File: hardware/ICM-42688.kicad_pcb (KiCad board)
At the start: 2 copper layers, 35 x 25 mm, 34 parts, among them J1 Conn_01x09, Q1 BSS138, Q2 BSS138, Q3 BSS138, Q4 BSS138, U1 AMS1117-3.3, U2 ICM-42688-P

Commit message: feat: Add panelized PCB files
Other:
- board text added: "Accelerometer & Gyroscope ICM-42688 SPI/I2C Breakout Board"
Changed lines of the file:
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@@
 		(tags "capacitor tantalum")
 		(property "Reference" "C3"
-			(at 0 2.015 360)
+			(at 0 2.015 0)
 			(layer "F.SilkS")
 			(effects
@@
 		)
 		(property "Value" "2.2uF"
-			(at 0 2.35 360)
+			(at 0 2.35 0)
 			(layer "F.Fab")
 			(effects
@@
 		)
 		(fp_text user "${REFERENCE}"
-			(at 0 0 360)
+			(at 0 0 0)
 			(layer "F.Fab")
 			(effects
@@
 		(layer "Edge.Cuts")
 	)
+	(gr_text "Accelerometer & Gyroscope\nICM-42688 SPI/I2C Breakout Board"
+		(at 137.5 83.968972 0)
+		(layer "B.SilkS")
+		(effects
+			(font
+				(size 1 1)
+				(thickness 0.2)
+				(bold yes)
+			)
+			(justify bottom mirror)
+		)
+	)
 	(gr_text "SPI: V+ 3V3 DOUT DIN SCLK CS INT1 INT2 GND\nI2C: V+ 3V3 ADDR SDA SCL  NC INT1 INT2 GND"

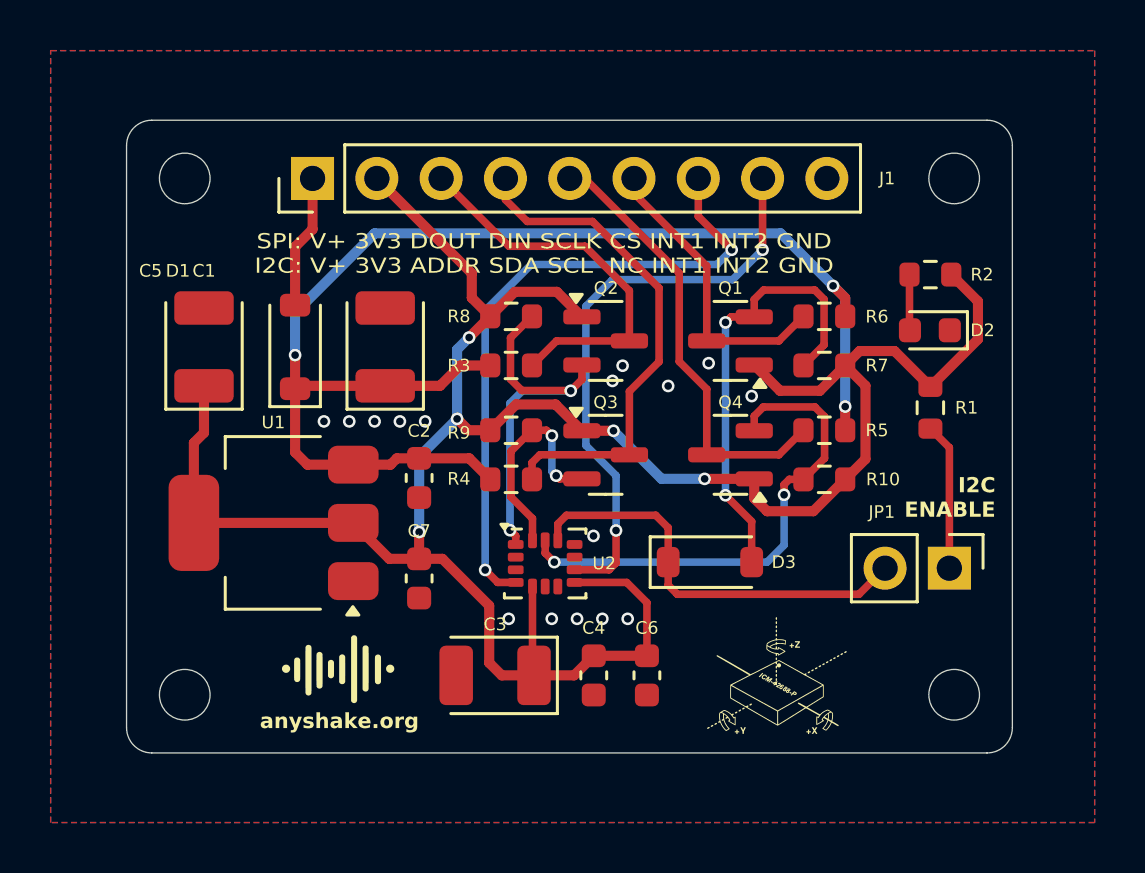
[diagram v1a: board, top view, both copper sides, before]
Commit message: fix: Fix SPI communication failure
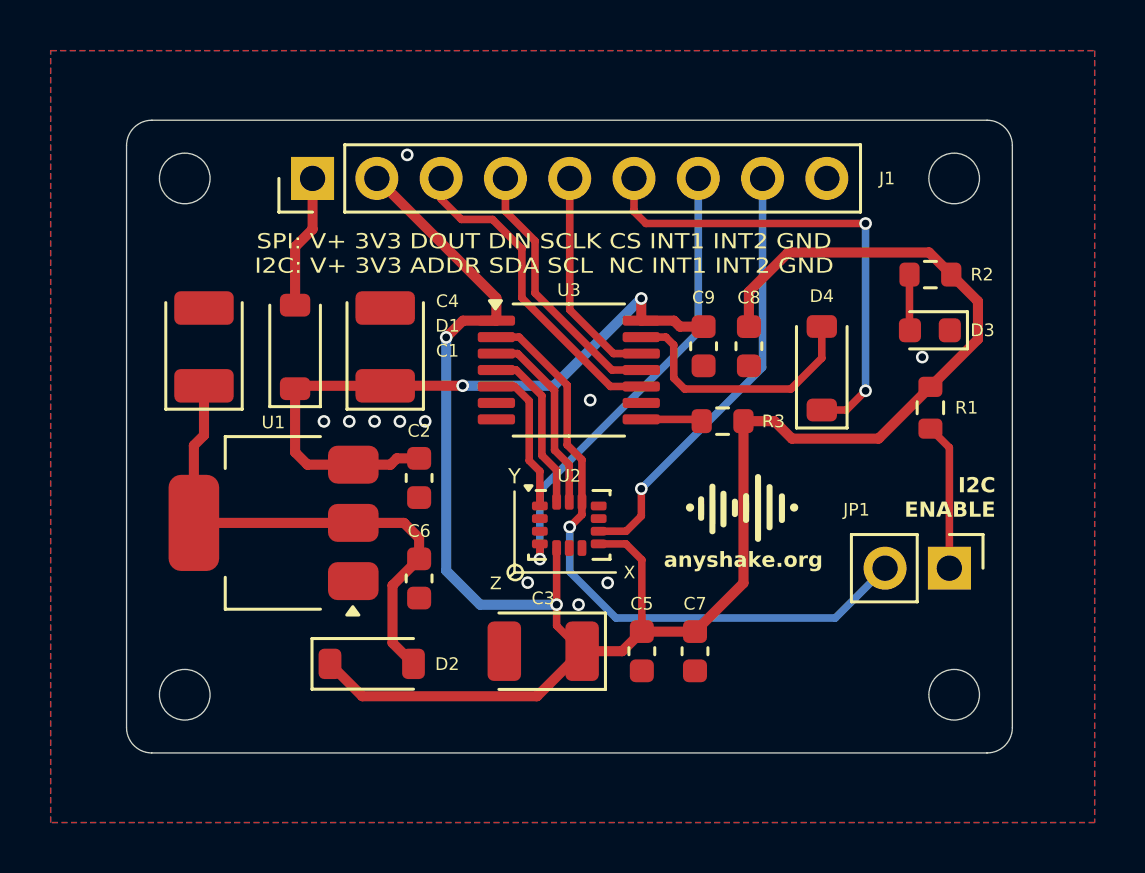
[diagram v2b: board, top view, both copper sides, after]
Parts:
- removed the D3 at (143.1, 87.5)
- removed the G*** at (145.8, 92.0)
- removed Q1, Q2, Q3, Q4: BSS138, Package_TO_SOT_SMD:SOT-23
- removed R10, R4, R5, R6, R7, R8, R9: 10k, Resistor_SMD:R_0603_1608Metric
- added C8: 0.1uF, Capacitor_SMD:C_0603_1608Metric, F.Cu at (144.6, 78.9)
- added C9: 0.1uF, Capacitor_SMD:C_0603_1608Metric, F.Cu at (142.8, 78.9)
- added D2: 1N4148, Diode_SMD:D_SOD-123, F.Cu at (129.7, 91.5)
- added D4: 1N4148, Diode_SMD:D_SOD-123, F.Cu at (147.5, 79.8)
- added U3: TXB0104PW, Package_SO:TSSOP-14_4.4x5mm_P0.65mm, F.Cu at (137.5, 79.9)
- R3: value 10k -> 4.7k
- moved G*** 17.2 mm to (144.3, 85.3)
- moved R3 8.64 mm to (143.6, 81.9)
- moved C3 2.13 mm to (136.5, 91.0)
- moved C5 2.13 mm to (140.4, 91.0)
- moved C7 2.13 mm to (142.5, 91.0)
- moved U2 1.80 mm to (137.5, 86.0)
- renumbered C5 to C4, C4 to C5, C7 to C6, C6 to C7, D2 to D3
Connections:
- net VCC renamed +5V
- C4 pad 1: +3V3 -> Net-(D2-A)
- C6 pad 1: +3V3 -> Net-(D2-A)
- R3 pad 1: VDD -> Net-(U3-OE)
- R3 pad 2: /DOUT_AD0 -> +3V3
- U1 pad 2: +3V3 -> Net-(D2-A)
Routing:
- net VDD: track 52.5 -> 26.2 mm, vias 3 -> 2
- net Net-(D2-A): track 0.00 -> 20.5 mm
- net Net-(D3-A) (its old number): track 17.8 -> 0.00 mm, vias 2 -> 0
- net +3V3: track 97.0 -> 82.9 mm, vias 5 -> 2
- net /SCL_SCLK_3V3: track 20.1 -> 7.54 mm, vias 2 -> 0
- net Net-(D4-A): track 0.00 -> 10.5 mm
- net /SDA_DIN: track 20.1 -> 10.5 mm
- net /DOUT_AD0_3V3: track 14.9 -> 5.86 mm, vias 2 -> 0
- net /AP_CS_3V3: track 16.8 -> 25.4 mm, vias 0 -> 1
- net /SCL_SCLK: track 17.1 -> 8.73 mm
- net /AP_CS: track 11.2 -> 19.3 mm, vias 0 -> 2
- net /INT1: track 25.8 -> 18.2 mm, vias 2 -> 1
- net /INT2: track 23.1 -> 17.3 mm, vias 2 -> 1
- net /DOUT_AD0: track 15.5 -> 12.9 mm
- net Net-(U3-OE): track 0.00 -> 2.42 mm
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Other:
- board text added: "X"
- board text added: "Y"
- board text added: "Z"
